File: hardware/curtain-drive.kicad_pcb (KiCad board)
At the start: 2 copper layers, 70 x 48 mm, 50 parts, among them J1 DC IN 12V, J2 USB-C, J3 MOTOR, J4 ENCODER I2C, SW1 USER, SW2 BOOT, SW3 RESET, U1 ESP32-C3-WROOM-02, U2 DRV8876PWP, U3 AP63203WU, U4 USBLC6-2SC6

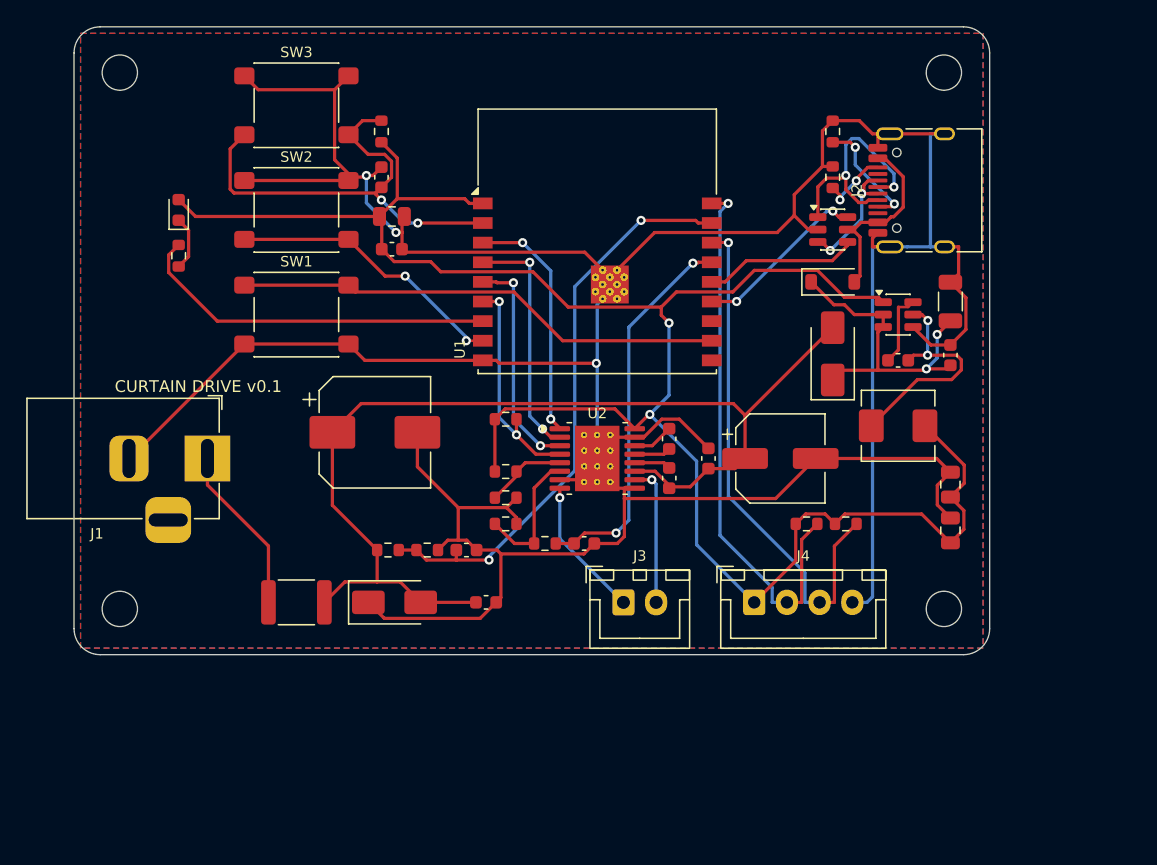
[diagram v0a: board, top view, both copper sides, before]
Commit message: Rev B through-hole board, rev A fixes, enclosure and renders
Rev B (hardware-revB/): same circuit and ESP32-C3 as rev A, but every
passive, diode, LED, switch and header is a through-hole part stocked by
the DTU component shop. Still single-sided with no vias: SMD parts on
F.Cu, THT bodies on the back. 90x72 mm, DRC clean. BOM mapped to shop
rows in docs/revB-bom.md.

Rev A: single-sided, via-free layout for the xTool fiber laser; D1 TVS
turned the right way round (cathode on +12V); R8 SCL pull-up 4.7k to
match SDA; production DXFs and drill.

Enclosure: Blender model, 3D board exports, showcase renders and GIFs.
Firmware: pin map for the new layout, vm_divider substitution.
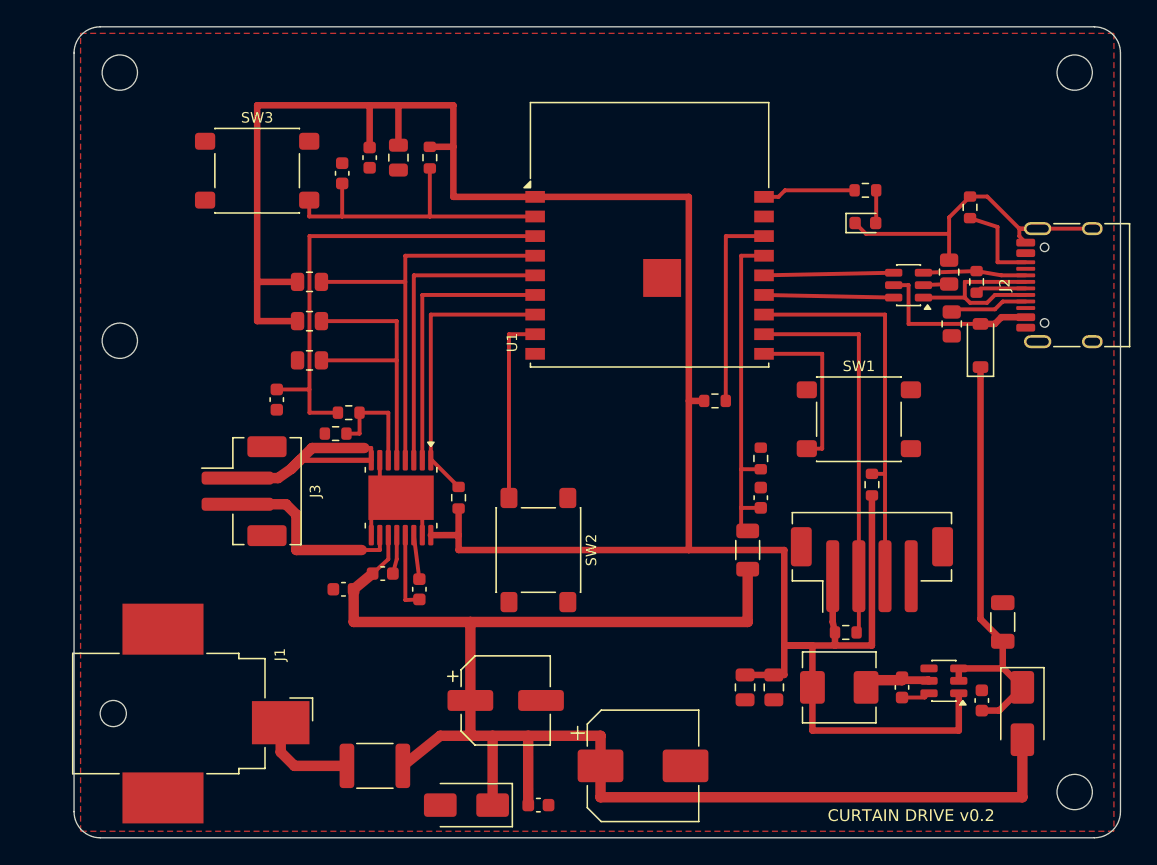
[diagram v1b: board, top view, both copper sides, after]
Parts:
- added R14: 0R, Resistor_SMD:R_0603_1608Metric, F.Cu at (169.0, 119.5)
- added R15: 10k, Resistor_SMD:R_0603_1608Metric, F.Cu at (149.0, 128.6)
- added R16: 0R, Resistor_SMD:R_0805_2012Metric, F.Cu at (166.9, 118.8)
- added R19: 10k, Resistor_SMD:R_0603_1608Metric, F.Cu at (129.4, 136.0)
- J1: footprint Connector_BarrelJack:BarrelJack_Horizontal -> Connector_BarrelJack:BarrelJack_CUI_PJ-036AH-SMT_Horizontal
- J2: footprint Connector_USB:USB_C_Receptacle_HRO_TYPE-C-31-M-12 -> CurtainDrive:USB_C_Receptacle_HRO_TYPE-C-31-M-12_1L
- J3: footprint Connector_JST:JST_XH_B2B-XH-A_1x02_P2.50mm_Vertical -> Connector_JST:JST_PH_B2B-PH-SM4-TB_1x02-1MP_P2.00mm_Vertical
- J4: footprint Connector_JST:JST_XH_B4B-XH-A_1x04_P2.50mm_Vertical -> Connector_JST:JST_PH_B4B-PH-SM4-TB_1x04-1MP_P2.00mm_Vertical
- R1: footprint Resistor_SMD:R_0603_1608Metric -> Resistor_SMD:R_1206_3216Metric
- R10, R13, R3, R9: footprint Resistor_SMD:R_0603_1608Metric -> Resistor_SMD:R_0805_2012Metric
- R8: value 10k -> 4.7k
- SW1, SW2, SW3: footprint Button_Switch_SMD:SW_SPST_PTS645Sx43SMTR92 -> CurtainDrive:SW_SPST_PTS645Sx43SMTR92_Jumpers
- U1: footprint RF_Module:ESP32-C3-WROOM-02 -> CurtainDrive:ESP32-C3-WROOM-02_NoVias
- U2: footprint Package_SO:HTSSOP-16-1EP_4.4x5mm_P0.65mm_EP3.4x5mm_Mask2.46x2.31mm_ThermalVias -> Package_SO:HTSSOP-16-1EP_4.4x5mm_P0.65mm_EP3.4x5mm_Mask2.46x2.31mm
- moved H3 74.3 mm to (176.5, 158.5)
- moved H4 66.3 mm to (103.5, 124.0)
- moved R6 52.7 mm to (160.5, 112.5), turned to 0 degrees
- moved D3 52.5 mm to (160.5, 115.0), turned to 0 degrees
- moved SW1 43.7 mm to (160.0, 130.0)
- moved C1 32.7 mm to (143.5, 156.5)
- moved SW2 31.9 mm to (135.5, 140.0), turned to -90 degrees
- moved D2 31.1 mm to (172.5, 152.5), turned to -90 degrees
- moved J3 30.2 mm to (113.0, 135.5), turned to -90 degrees
- moved C15 29.6 mm to (120.6, 143.0), turned to 180 degrees
- moved U3 28.2 mm to (166.5, 150.0), turned to 180 degrees
- moved C16 28.0 mm to (133.0, 151.5)
- moved R1 27.5 mm to (151.5, 140.0), turned to 90 degrees
- moved C5 26.5 mm to (169.4, 151.5)
- moved R2 26.4 mm to (152.5, 133.0), turned to 90 degrees
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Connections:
- D1 pad 1: GND -> +12V
- D1 pad 2: +12V -> GND
- D3 pad 1: Net-(D3-K) -> GND
- D3 pad 2: +3V3 -> Net-(D3-A)
- J2 pad B6: Net-(J2-D+-PadA6) -> Net-(J2-D+-PadB6)
- R6 pad 1: Net-(D3-K) -> LED
- R6 pad 2: Net-(U1-IO8) -> Net-(D3-A)
- SW1 pad 1: Net-(U1-IO20/RXD) -> GND
- SW1 pad 2: GND -> Net-(U1-IO10)
- U1 pad 10: unconnected-(U1-IO10-Pad10) -> Net-(U1-IO10)
- U1 pad 11: Net-(U1-IO20/RXD) -> SDA
- U1 pad 12: unconnected-(U1-IO21/TXD-Pad12) -> SCL
- U1 pad 15: I_SENSE -> VM_SENSE
- U1 pad 16: SCL -> Net-(U1-IO2)
- U1 pad 17: VM_SENSE -> unconnected-(U1-IO1-Pad17)
- U1 pad 18: SDA -> LED
- U1 pad 3: M_IN1 -> I_SENSE
- U1 pad 4: M_IN2 -> M_nFAULT
- U1 pad 6: M_nFAULT -> M_IN2
- U1 pad 7: Net-(U1-IO8) -> M_IN1
- U4 pad 2: GND -> Net-(U4-GND)
- U4 pad 3: Net-(J2-D+-PadA6) -> Net-(J2-D+-PadB6)
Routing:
- net GND: track 313.2 -> 30.9 mm, vias 3 -> 0
- net Net-(U1-IO20/RXD): track 37.5 -> 0.00 mm
- net +12V: track 81.3 -> 118.6 mm
- net +3V3: track 150.7 -> 187.9 mm, vias 2 -> 0
- net Net-(U1-IO8): track 28.0 -> 0.00 mm
- net VM_SENSE: track 44.3 -> 26.3 mm, vias 2 -> 0
- net Net-(U2-VREF): track 6.28 -> 22.2 mm
- net Net-(U1-IO2): track 0.00 -> 15.5 mm
- net M_nFAULT: track 17.1 -> 32.0 mm, vias 2 -> 0
- net Net-(U1-IO10): track 0.00 -> 12.9 mm
- net Net-(U3-SW): track 17.8 -> 5.29 mm, vias 2 -> 0
- net SDA: track 42.4 -> 30.2 mm, vias 1 -> 0
- net Net-(U1-EN): track 35.1 -> 24.7 mm, vias 2 -> 0
- net SCL: track 40.2 -> 30.2 mm, vias 1 -> 0
- net /VBUCK: track 24.9 -> 34.0 mm, vias 2 -> 0
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- removed copper zone on B.Cu, net GND
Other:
- board size 70 x 48 mm -> 80 x 62 mm
- board text added: "CURTAIN DRIVE v0.2"
- board text removed: "CURTAIN DRIVE v0.1"
